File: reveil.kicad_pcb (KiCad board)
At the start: 2 copper layers, 168.5 x 143 mm, 13 parts, among them SW2 SW_Push, U1 MAX7219, U2 MAX7219

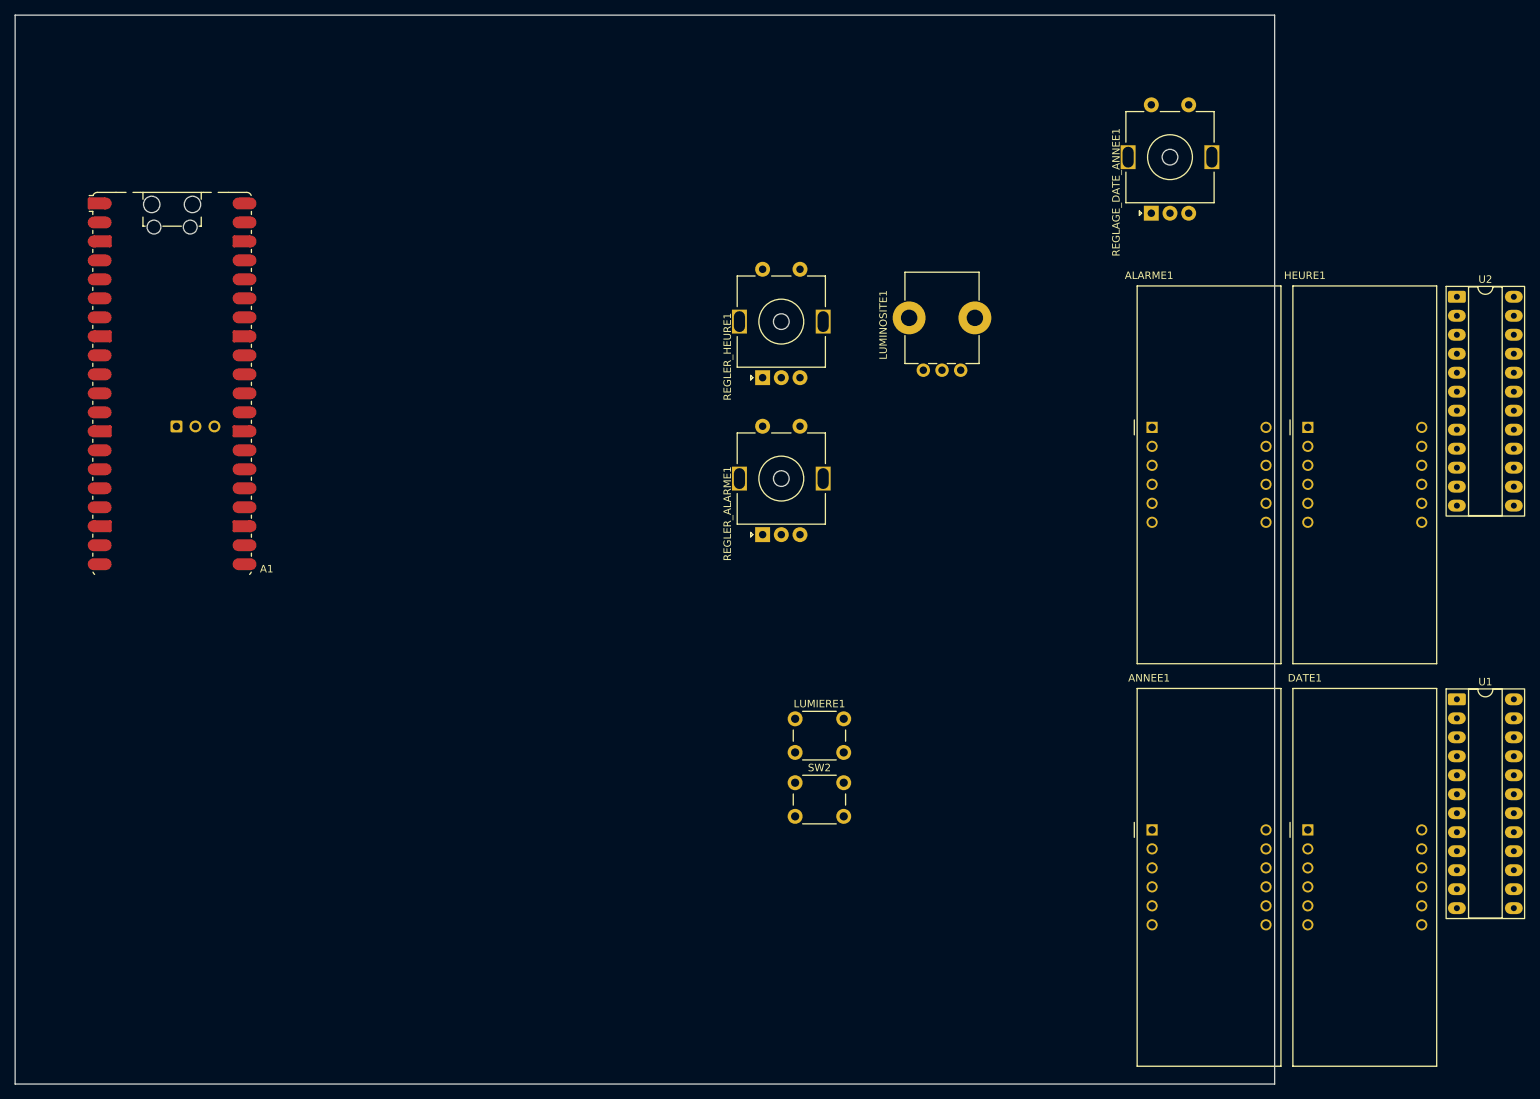
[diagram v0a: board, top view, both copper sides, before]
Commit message: Added VBUS and misc
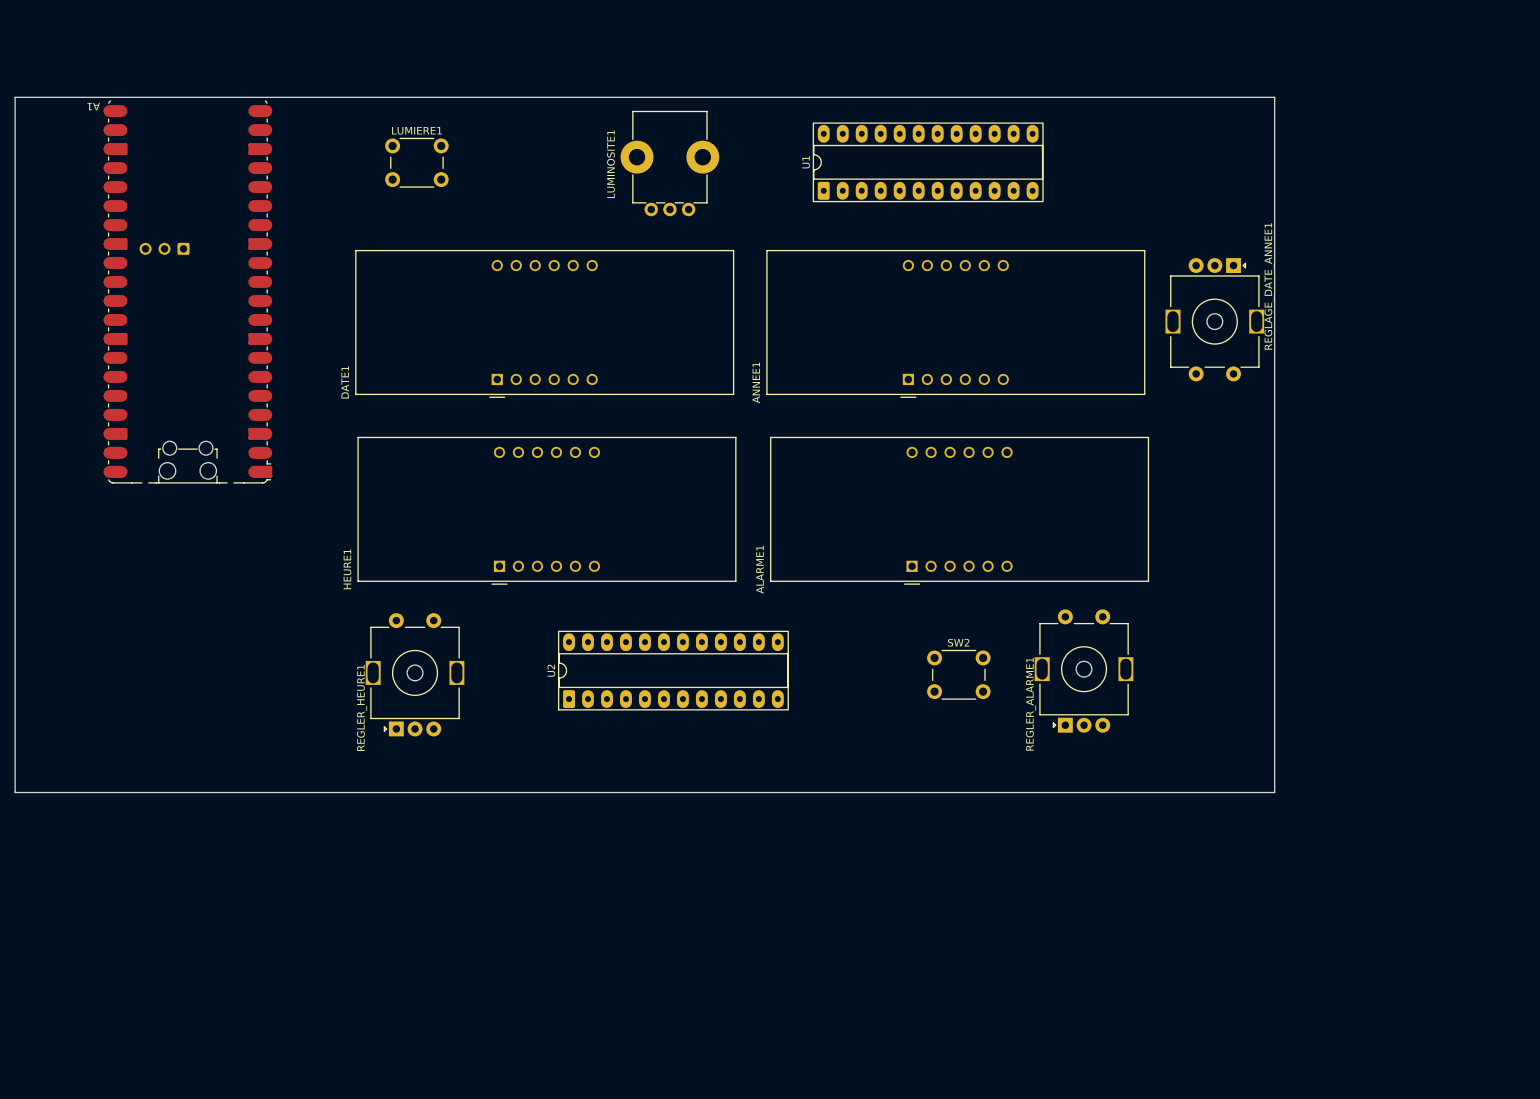
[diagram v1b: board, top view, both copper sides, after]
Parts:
- moved U2 130.4 mm to (148.6, 100.5), turned to 90 degrees
- moved DATE1 124.1 mm to (139.0, 57.7), turned to 90 degrees
- moved HEURE1 109.7 mm to (139.3, 82.7), turned to 90 degrees
- moved U1 108.6 mm to (182.7, 32.5), turned to 90 degrees
- moved LUMIERE1 93.7 mm to (125.0, 26.5)
- moved ANNEE1 68.5 mm to (194.0, 57.7), turned to 90 degrees
- moved REGLER_HEURE1 67.9 mm to (125.5, 104.5)
- moved REGLER_ALARME1 47.9 mm to (215.0, 104.0)
- moved LUMINOSITE1 42.3 mm to (164.6, 35.0)
- moved ALARME1 37.1 mm to (194.5, 82.7), turned to 90 degrees
- moved SW2 25.0 mm to (197.5, 95.0)
- moved REGLAGE_DATE_ANNEE1 13.0 mm to (237.5, 42.5), turned to -90 degrees
- moved A1 12.5 mm to (97.6, 46.0), turned to 180 degrees
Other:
- board size 168.5 x 143 mm -> 168.5 x 93 mm

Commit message: un peu plus de composants connectés
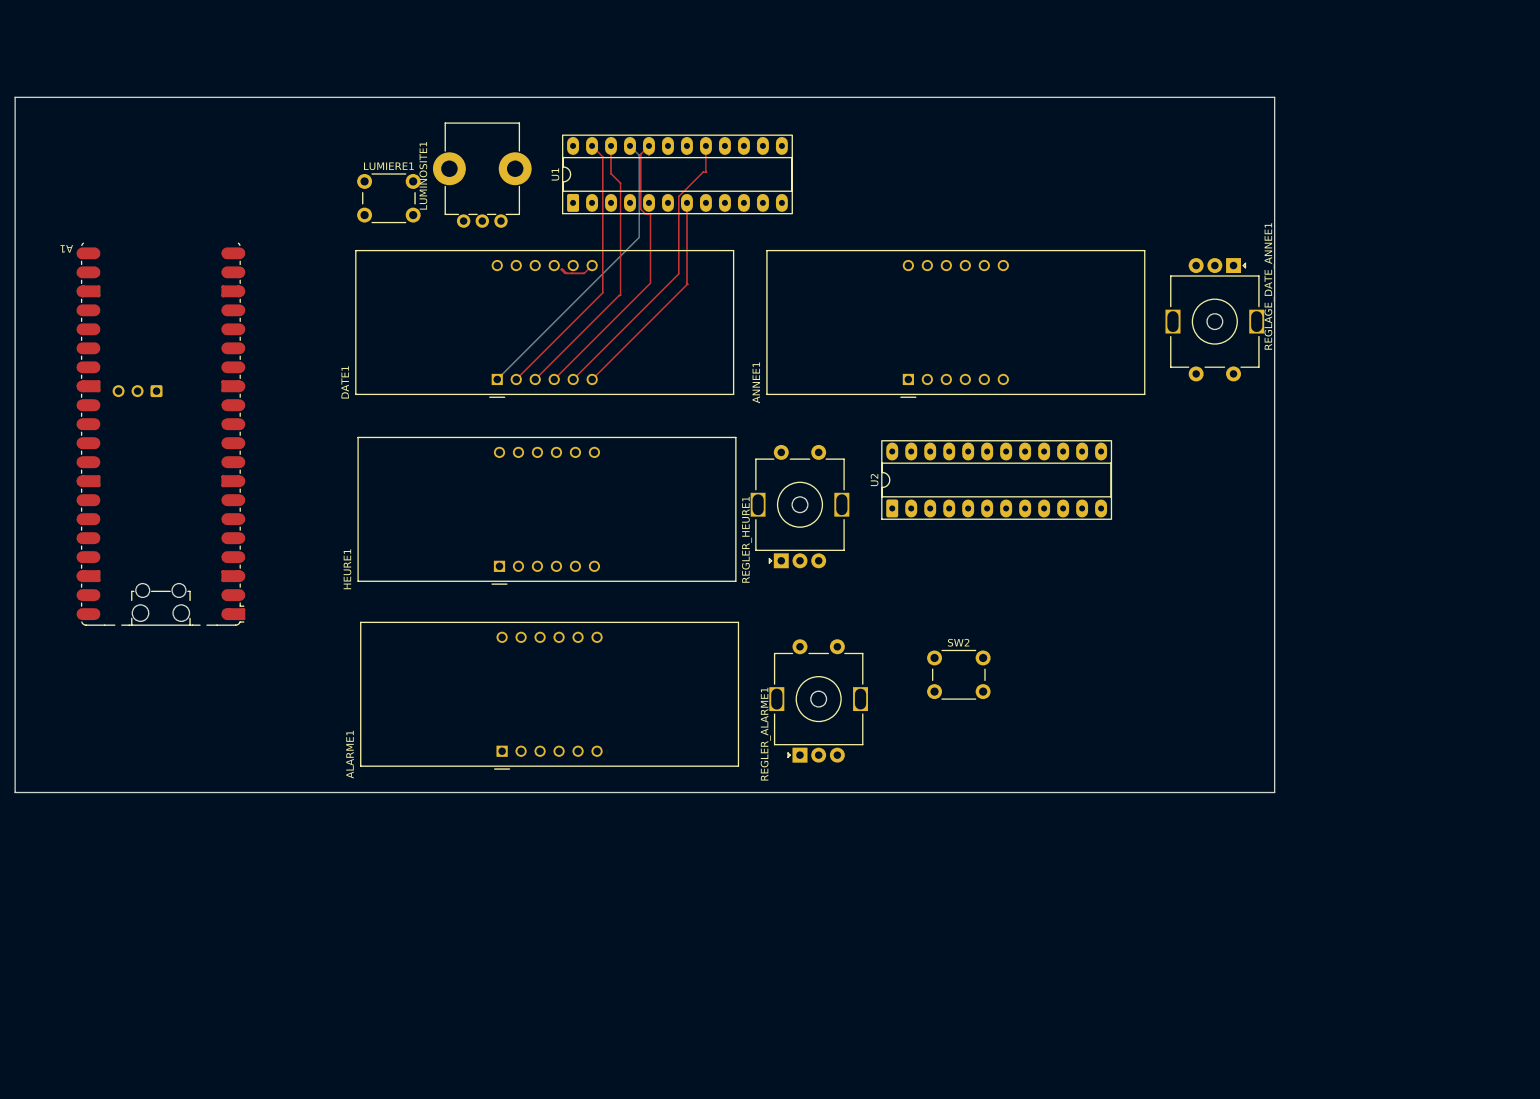
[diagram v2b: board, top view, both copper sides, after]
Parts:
- moved ALARME1 60.2 mm to (139.7, 107.5)
- moved REGLER_HEURE1 56.2 mm to (177.0, 82.0)
- moved U2 50.2 mm to (191.8, 75.0)
- moved REGLER_ALARME1 35.7 mm to (179.5, 108.0)
- moved U1 33.6 mm to (149.1, 34.1)
- moved LUMINOSITE1 25.1 mm to (139.5, 36.5)
- moved A1 19.4 mm to (94.0, 65.0)
- moved LUMIERE1 6.05 mm to (121.2, 31.2)
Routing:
- net Net-(ANNEE1-e): track 0.00 -> 39.6 mm
- net Net-(ANNEE1-c): track 0.00 -> 39.3 mm
- net Net-(ANNEE1-g): track 0.00 -> 38.9 mm
- net Net-(ANNEE1-d): track 0.00 -> 36.6 mm
- net Net-(ANNEE1-DPX): track 0.00 -> 36.6 mm
- net Net-(DATE1-CA4): track 0.00 -> 29.0 mm
- net Net-(ANNEE1-b): track 0.00 -> 8.13 mm

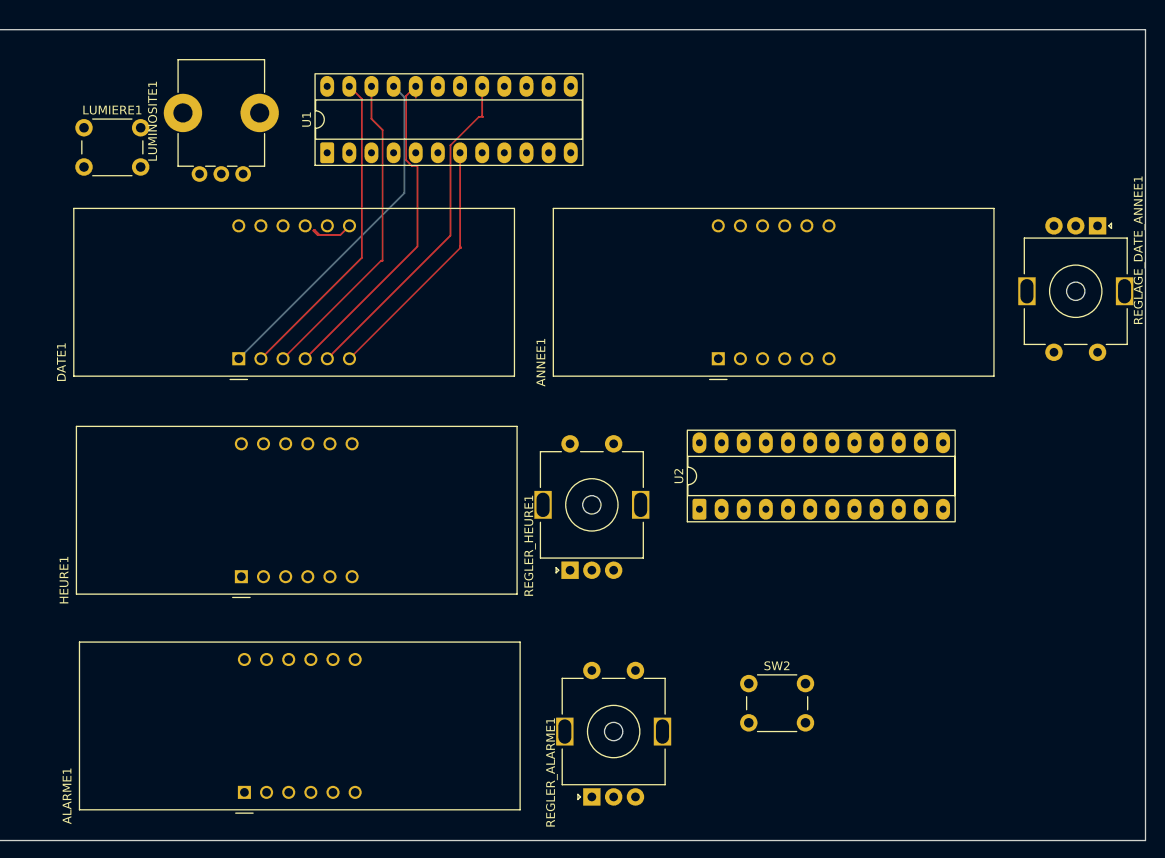
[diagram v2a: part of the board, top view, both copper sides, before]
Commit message: tous les composants sont ajoutés et connecté dans le schema
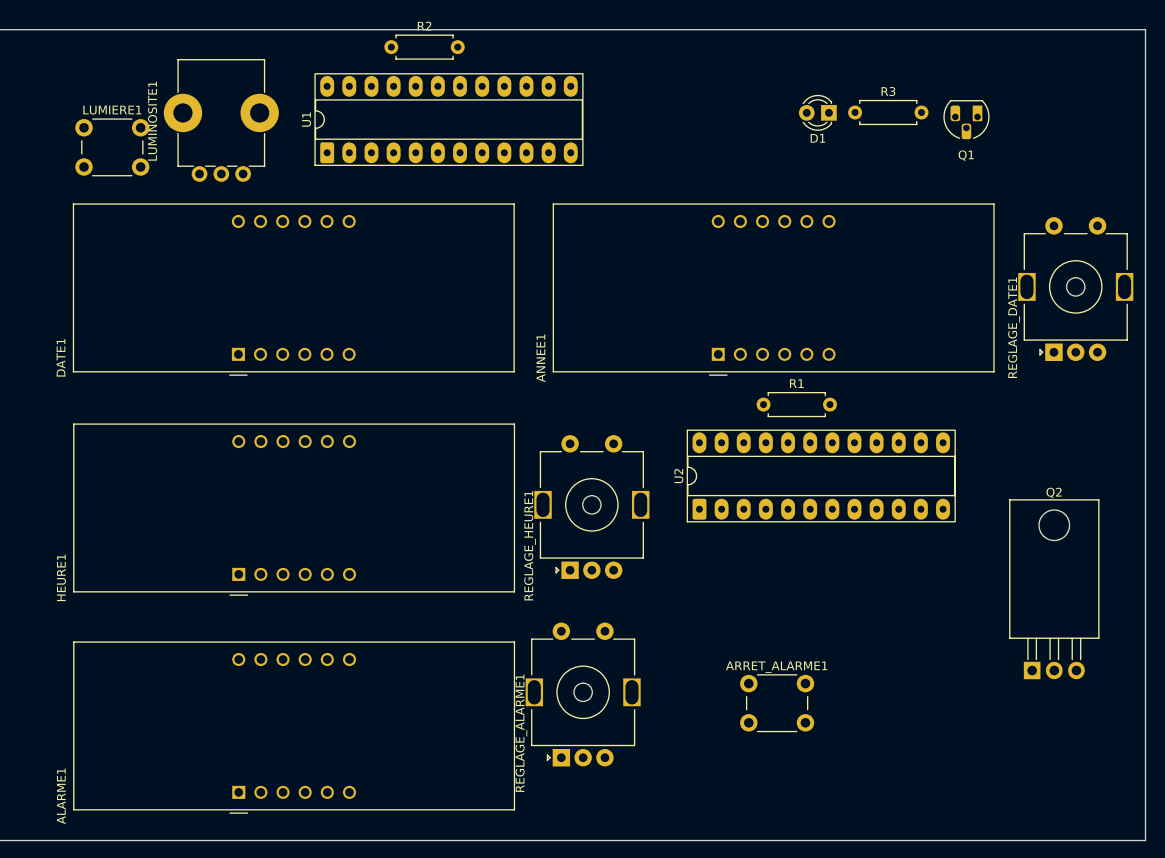
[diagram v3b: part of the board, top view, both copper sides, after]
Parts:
- removed REGLAGE_DATE_ANNEE1, REGLER_ALARME1: RotaryEncoder_Switch_MP, Rotary_Encoder:RotaryEncoder_Alps_EC11E-Switch_Vertical_H20mm_MountingHoles
- added D1: LED, LED_THT:LED_D3.0mm, F.Cu at (206.7, 29.5)
- added Q1: 2N3904, Package_TO_SOT_THT:TO-92_HandSolder, F.Cu at (223.7, 30.0)
- added Q2: IRF540N, Package_TO_SOT_THT:TO-220-3_Horizontal_TabDown, F.Cu at (230.0, 93.5)
- added R1: R, Resistor_THT:R_Axial_DIN0207_L6.3mm_D2.5mm_P7.62mm_Horizontal, F.Cu at (199.2, 63.0)
- added R2: R, Resistor_THT:R_Axial_DIN0207_L6.3mm_D2.5mm_P7.62mm_Horizontal, F.Cu at (156.5, 22.0)
- added R3: R, Resistor_THT:R_Axial_DIN0207_L6.3mm_D2.5mm_P7.62mm_Horizontal, F.Cu at (209.7, 29.5)
- added REGLAGE_ALARME1: RotaryEncoder_Switch_MP, Rotary_Encoder:RotaryEncoder_Alps_EC11E-Switch_Vertical_H20mm_MountingHoles, F.Cu at (176.0, 103.5)
- added REGLAGE_DATE1: RotaryEncoder_Switch_MP, Rotary_Encoder:RotaryEncoder_Alps_EC11E-Switch_Vertical_H20mm_MountingHoles, F.Cu at (232.5, 57.0)
- moved ALARME1 0.65 mm to (139.0, 107.5)
- moved DATE1 0.50 mm to (139.0, 57.2)
- moved ANNEE1 0.50 mm to (194.0, 57.2)
- moved HEURE1 0.40 mm to (139.0, 82.5)
- renumbered SW2 to ARRET_ALARME1, REGLER_HEURE1 to REGLAGE_HEURE1
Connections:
- A1 pad 1: unconnected-(A1-GPIO0-Pad1) -> REGLAGE_HEURE_A
- A1 pad 11: unconnected-(A1-GPIO8-Pad11) -> REGLAGE_DATE_S
- A1 pad 12: unconnected-(A1-GPIO9-Pad12) -> DATE_LOAD
- A1 pad 13: Net-(A1-GND-Pad13) -> GND
- A1 pad 14: unconnected-(A1-GPIO10-Pad14) -> DATE_CLK
- A1 pad 15: unconnected-(A1-GPIO11-Pad15) -> DATE_DIN
- A1 pad 16: unconnected-(A1-GPIO12-Pad16) -> REGLAGE_ALARME_A
- A1 pad 17: unconnected-(A1-GPIO13-Pad17) -> REGLAGE_ALARME_B
- A1 pad 18: Net-(A1-GND-Pad13) -> GND
- A1 pad 19: unconnected-(A1-GPIO14-Pad19) -> REGLAGE_ALARME_S
- A1 pad 2: unconnected-(A1-GPIO1-Pad2) -> REGLAGE_HEURE_B
- A1 pad 20: unconnected-(A1-GPIO15-Pad20) -> LUMIERE
- A1 pad 21: unconnected-(A1-GPIO16-Pad21) -> ARRET_ALARME
- A1 pad 22: unconnected-(A1-GPIO17-Pad22) -> LED
- A1 pad 23: Net-(A1-GND-Pad13) -> GND
- A1 pad 24: unconnected-(A1-GPIO18-Pad24) -> VIBREUR
- A1 pad 28: Net-(A1-GND-Pad13) -> GND
- A1 pad 3: Net-(A1-GND-Pad13) -> GND
- A1 pad 31: unconnected-(A1-GPIO26_ADC0-Pad31) -> LUMINOSITE
- A1 pad 33: unconnected-(A1-AGND-Pad33) -> GND
- A1 pad 36: unconnected-(A1-3V3-Pad36) -> +3V3
- A1 pad 38: Net-(A1-GND-Pad13) -> GND
- A1 pad 4: unconnected-(A1-GPIO2-Pad4) -> REGLAGE_HEURE_S
- A1 pad 40: unconnected-(A1-VBUS-Pad40) -> VBUS
- A1 pad 5: unconnected-(A1-GPIO3-Pad5) -> REGLAGE_DATE_A
- A1 pad 6: unconnected-(A1-GPIO4-Pad6) -> REGLAGE_DATE_B
- A1 pad 8: Net-(A1-GND-Pad13) -> GND
- ARRET_ALARME1 pad 1: unconnected-(SW2-Pad1) -> ARRET_ALARME
- ARRET_ALARME1 pad 2: unconnected-(SW2-Pad2) -> GND
- LUMIERE1 pad 1: unconnected-(LUMIERE1-Pad1) -> LUMIERE
- LUMIERE1 pad 2: unconnected-(LUMIERE1-Pad2) -> GND
- LUMINOSITE1 pad 1: unconnected-(LUMINOSITE1-Pad1) -> +3V3
- LUMINOSITE1 pad 2: unconnected-(LUMINOSITE1-Pad2) -> LUMINOSITE
- LUMINOSITE1 pad 3: unconnected-(LUMINOSITE1-Pad3) -> GND
- LUMINOSITE1 pad MP: unconnected-(LUMINOSITE1-MountPin-PadMP) -> GND
- REGLAGE_HEURE1 pad A: unconnected-(REGLER_HEURE1-PadA) -> REGLAGE_HEURE_A
- REGLAGE_HEURE1 pad B: unconnected-(REGLER_HEURE1-PadB) -> REGLAGE_HEURE_B
- REGLAGE_HEURE1 pad C: unconnected-(REGLER_HEURE1-PadC) -> GND
- REGLAGE_HEURE1 pad MP: unconnected-(REGLER_HEURE1-PadMP) -> GND
- REGLAGE_HEURE1 pad S1: unconnected-(REGLER_HEURE1-PadS1) -> REGLAGE_HEURE_S
- REGLAGE_HEURE1 pad S2: unconnected-(REGLER_HEURE1-PadS2) -> GND
- U1 pad 19: VCC -> VBUS
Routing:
- net Net-(ANNEE1-e): track 39.6 -> 0.00 mm
- net Net-(ANNEE1-c): track 39.3 -> 0.00 mm
- net Net-(ANNEE1-g): track 38.9 -> 0.00 mm
- net Net-(ANNEE1-d): track 36.6 -> 0.00 mm
- net Net-(ANNEE1-DPX): track 36.6 -> 0.00 mm
- net Net-(DATE1-CA4): track 29.0 -> 0.00 mm
- net Net-(ANNEE1-b): track 8.13 -> 0.00 mm

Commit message: decoupling caps
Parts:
- added C1: 100nF, Capacitor_THT:C_Disc_D3.0mm_W1.6mm_P2.50mm, F.Cu at (214.0, 100.0)
- added C2: 10uF, Capacitor_THT:CP_Radial_D7.5mm_P2.50mm, F.Cu at (215.9, 93.9)
- added C3: 100nF, Capacitor_THT:C_Disc_D3.0mm_W1.6mm_P2.50mm, F.Cu at (222.0, 106.0)
- added C4: 10uF, Capacitor_THT:CP_Radial_D7.5mm_P2.50mm, F.Cu at (223.9, 99.9)
- R2: value R -> 47K

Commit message: contour du PCB
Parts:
- added REF**: OSHW-Logo_5.7x6mm_SilkScreen, Symbol:OSHW-Logo_5.7x6mm_SilkScreen, F.Cu at (225.0, 97.0)
- added REF**: KiCad-Logo2_5mm_SilkScreen, Symbol:KiCad-Logo2_5mm_SilkScreen, F.Cu at (237.5, 97.0)
- added SW1: SW_SPDT, Button_Switch_THT:SW_Slide-03_Wuerth-WS-SLTV_10x2.5x6.4_P2.54mm, F.Cu at (199.5, 96.5)
- moved C1 77.2 mm to (183.0, 29.2), turned to -90 degrees
- moved C2 68.9 mm to (191.5, 29.5), turned to -90 degrees
- moved C3 30.8 mm to (209.2, 78.0)
- moved C4 29.2 mm to (201.7, 81.0), turned to 180 degrees
- moved Q2 25.9 mm to (239.0, 69.3), turned to 180 degrees
- moved Q1 24.7 mm to (199.4, 34.0), turned to 0 degrees
- moved ARRET_ALARME1 12.5 mm to (210.0, 94.0)
- moved D1 12.1 mm to (217.7, 34.5), turned to 0 degrees
- moved ALARME1 7.70 mm to (131.5, 105.7)
- moved HEURE1 7.65 mm to (131.5, 84.0)
- moved DATE1 7.48 mm to (131.5, 56.7)
- moved R3 7.10 mm to (214.7, 34.5), turned to 180 degrees
- moved LUMIERE1 5.10 mm to (120.2, 26.2)
- moved REGLAGE_DATE1 4.74 mm to (237.1, 55.9)
- moved REGLAGE_ALARME1 1.33 mm to (177.0, 104.4)
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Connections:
- A1 pad 25: unconnected-(A1-GPIO19-Pad25) -> ALARME_ON_OFF
- U2 pad 19: VCC -> VBUS
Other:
- board size 168.5 x 93 mm -> 170 x 90 mm
- board text added: "Réveil pour sourd Oscar Lederrey V1.0"
